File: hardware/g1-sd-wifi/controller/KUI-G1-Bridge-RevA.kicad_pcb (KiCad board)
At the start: 6 copper layers, 59 x 115 mm, 351 parts, among them J10 FPGA JTAG pogo pads, J20 5V/GND direct wire pads, J201 microSD push-pull 1.42mm, J202 RP USB service pads, J203 RP SWD/reset/boot pads, J204 C5 direct UART recovery pads, J40 FH12-14S-0.5SH(55), J41 FH12-6S-0.5SH(55), J50 FH12-20S-0.5SH(55), J51 FH12-20S-0.5SH(55), K201 C5 removable compression cont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, K202 C5 removable compression cont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, K203 C5 removable compression cont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, K204 C5 removable compression cont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, K205 C5 removable compression cont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, K206 C5 removable compression cont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, K207 C5 removable compression cont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, K208 C5 removable compression cont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, K209 C5 removable compression cont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, K210 C5 removable compression cont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, K211 C5 removable compression cont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, K212 C5 removable compression cont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, K213 C5 removable compression cont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, K214 C5 removable compression cont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, K215 C5 removable compression cont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, K216 C5 removable compression cont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, Q20 PMV48XP reverse polarity, Q201 C5 recovery pull-down, Q202 C5 recovery pull-down, U10 LCMXO2-2000HC-4TG100C, U20 TPS2116 automatic mux, U201 RP2350B, U202 16MiB boot NOR, U203 8MiB QSPI PSRAM, U204 C5 off-state isolation, U205 C5 off-state isolation, U207 SD4-bit DAT rail isolation, U208 SD CLK/CMD rail isolation, U209 SD enable/power-good NAND, U21 TPS62162 3.3V 1A, U22 TPS62162 3.3V 1A, U23 TPS3808G33DBVR, U24 TPS3808G33DBVR, U25 TPS3808G33DBVR, U26 TPS3808G01DBVR, U27 SN74LVC2G08DCUR, U28 SN74LVC2G08DCUR, U29 SN74LVC2G08DCUR, U30 SN74LVC1G11DBVR, U31 SN74LVC2G04DBVT, U32 SN74LVC1G32DBVR, U33 SN74LVC1G08DBVR, U34 SN74LVC1G08DBVR, U35 SN74LVC16T245, U36 SN74LVC244A host controls, U37 SN74LVC1G17 host RESETn, U38 SN74LVC1G125 qualified ATA_IN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, U39 SN74LVC1G125 qualified ATA_DM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, U40 MX29LV640ETTI-70G x8 / 4 x 2M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, U41 SN74LVC2G125 bank-domain buff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, U42 SN74LVC1G11 write-authorize A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, U43 SN74LVC1G04 write-block inver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, U44 SN74LVC1G332 NOR WE qualifier, U45 TLV803EB29 console-rail NOR r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, U70 SN74LVC1G07 open-drain IORDY, U71 TPS22919 Wi-Fi input switch, U72 SN74LVC1G32DBVR, U73 SN74LVC1G32DBVR, X10 50MHz 3.3V, X201 12MHz

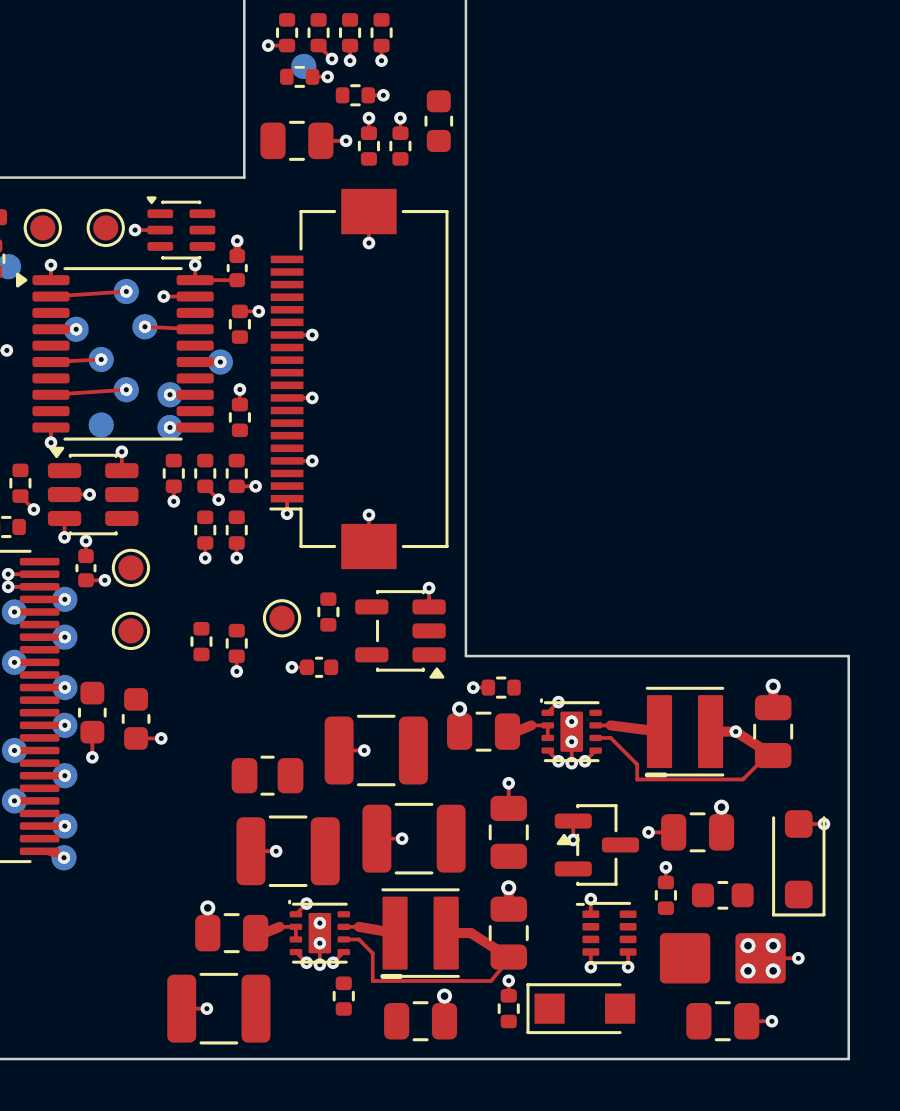
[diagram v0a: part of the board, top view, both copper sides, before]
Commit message: G1 safety: supply trunks laid first; current checker no longer passes vacuously
check_power_copper.py joined a track end that met another segment to both
of that segment's ends, collapsing most supply nets into a single node: the
source and loads merged, every branch carried 0 A and the check passed. The
copper graph now splits a track where another end or via lands on it, and
the 2x pad-escape allowance applies only to a short run that starts at a
pad, not to every short segment of a long track. On the last routed
snapshot this exposes the 1.3 A input path at 0.25-0.30 mm (about 25 C rise)
and a 0.2 mm via carrying the PRIMARY_5V trunk.

route_power_trunks.py now lays the high-current trunks on the placed board
before signal routing, locked: J20 -> F20 -> Q20 at 1.0 mm on F.Cu with no
via, F20 -> D21 at 0.8 mm, Q20 -> U20 at 0.5 mm with a short neck at the
fine-pitch pin, Q20 -> U71/C235 and Q20 -> C200 at 0.6-0.8 mm, as a tree.
C208 moves 1.2 mm towards L20 to open the input corridor.

Routing rules go to 0.127 mm track and space (0.15 mm stalled near 20 open
connections). close_gaps.py takes its rules from the project, rasterises
obstacles at the right cell offset (Pillow samples pixel centres at +0.5),
routes supply gaps only at supply widths with POWER vias, refills zones in
its DRC check, never saves a board without its project file, and gains a
rip-up mode in which each attempt is kept only if native DRC shows fewer
open connections and no new violation. The finishing script fails if the
project rules file changes.

Co-Authored-By: Claude Opus 5.5 <noreply@anthropic.com>
Claude-Session: https://claude.ai/code/session_01Gp9EYc2r9fMpZ7V8WtfonZ
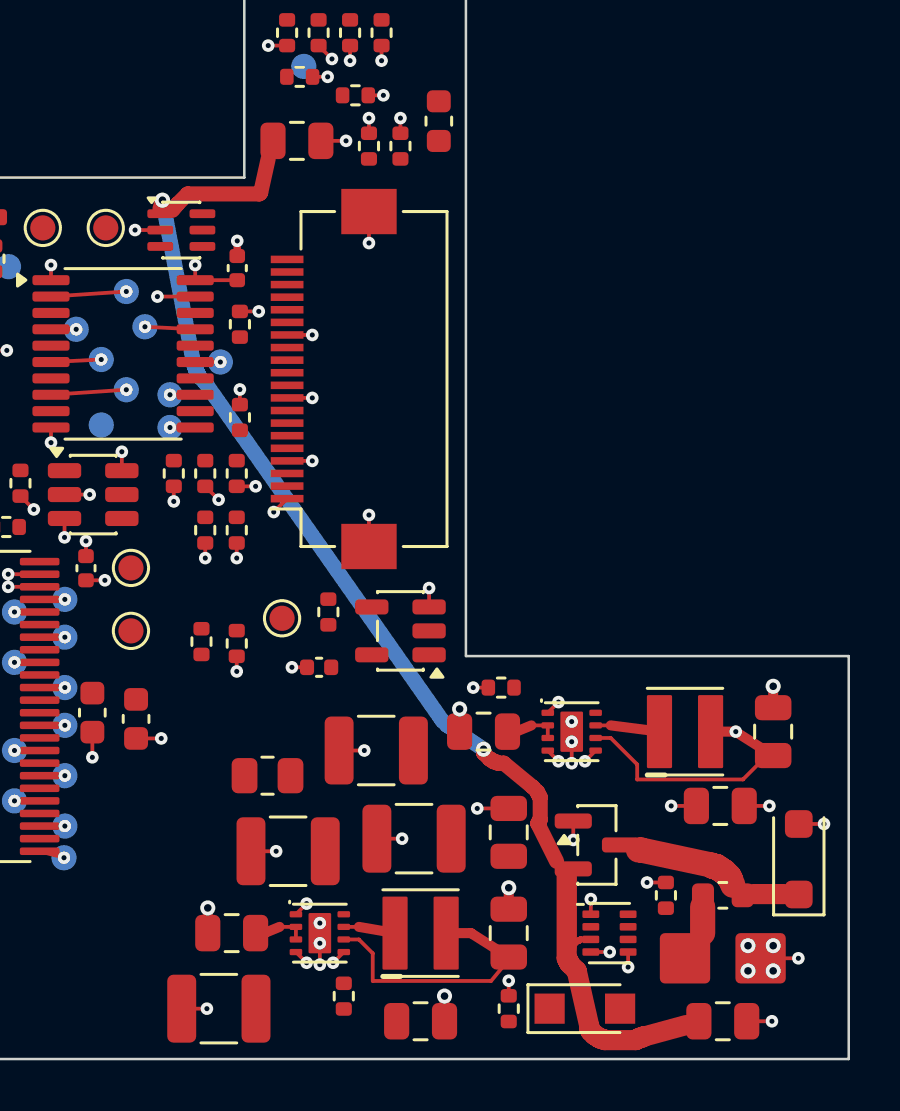
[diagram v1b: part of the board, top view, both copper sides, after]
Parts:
- moved C208 1.38 mm to (123.9, 149.9)
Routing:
- net PRIMARY_5V: track 0.00 -> 51.3 mm, vias 0 -> 2
- net FUSED_5V: track 0.00 -> 5.49 mm
- net CONSOLE_5V: track 0.00 -> 1.05 mm
- net GND: track 220.4 -> 221.2 mm

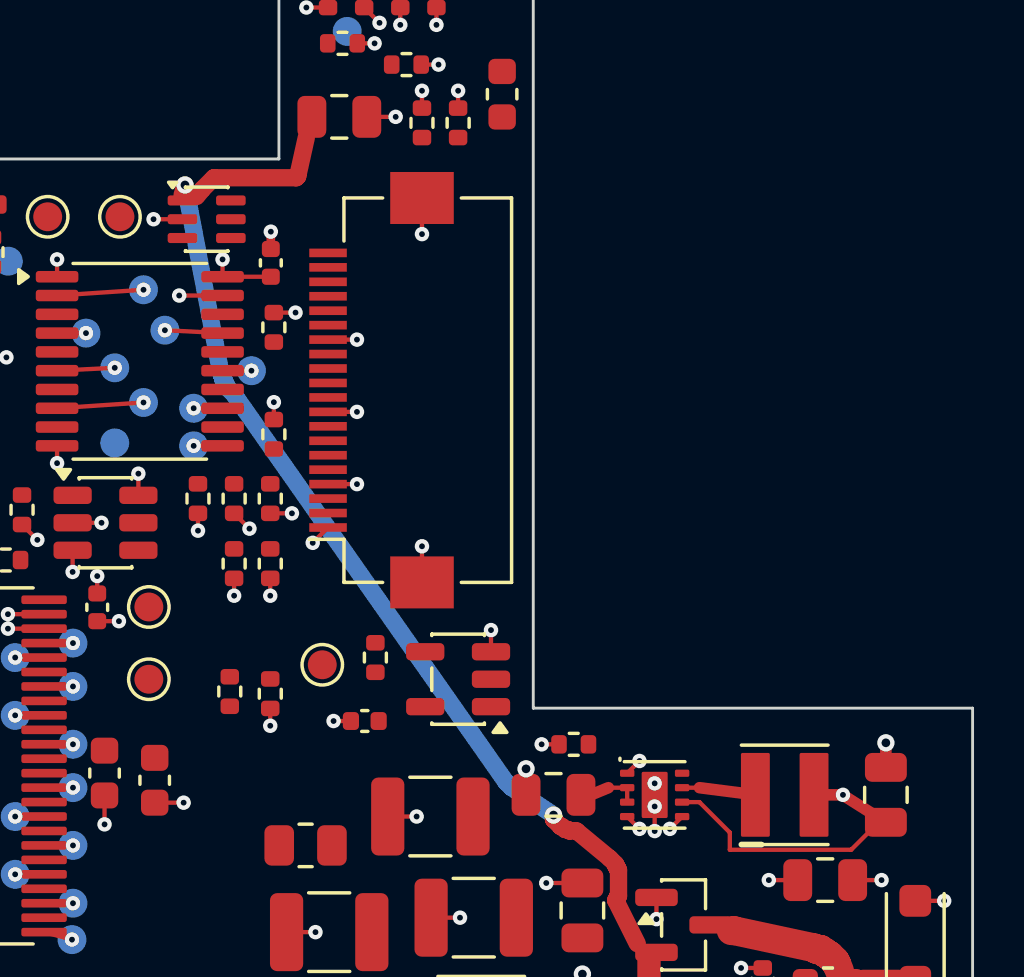
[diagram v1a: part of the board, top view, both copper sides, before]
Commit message: G1: resumable routing checkpoint; plane feed vias; rip-up can move vias
design/routing-checkpoint/ holds the board's DSN, the best routed session
and the SHA-256 of the board it belongs to; tools/route_carrier.sh starts,
resumes, saves and finishes from it, so a new session or container carries
on instead of routing again. design/ROUTING-CHECKPOINT.md records the state
and the remaining steps.

The +3V3_LOGIC plane was fed from L20.2 through one 0.2 mm via, about
108 C over ambient at the converter's assumed 1.5 A short-circuit current.
route_power_trunks.py now adds three 0.3 mm feed vias beside the pad (not
in it, so no solder is drawn from the joint), and check_power_copper.py
rates the plane feed at that fault current. close_gaps.py keeps new vias
0.1 mm clear of every SMD land, and its rip-up attempts may cut vias as
well as tracks, rerouting what native DRC then reports open.

Co-Authored-By: Claude Opus 5.5 <noreply@anthropic.com>
Claude-Session: https://claude.ai/code/session_01Gp9EYc2r9fMpZ7V8WtfonZ
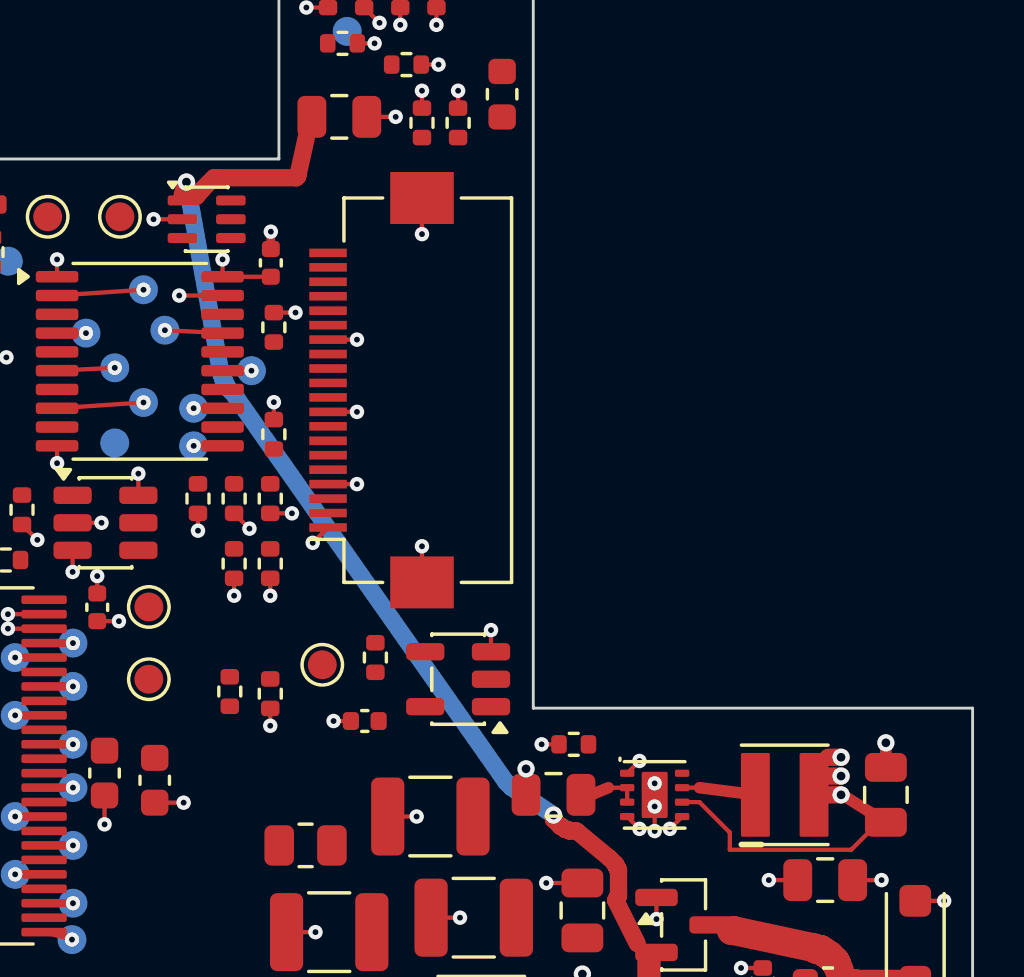
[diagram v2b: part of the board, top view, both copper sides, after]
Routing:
- net +3V3_LOGIC: track 145.3 -> 145.6 mm, vias 121 -> 123

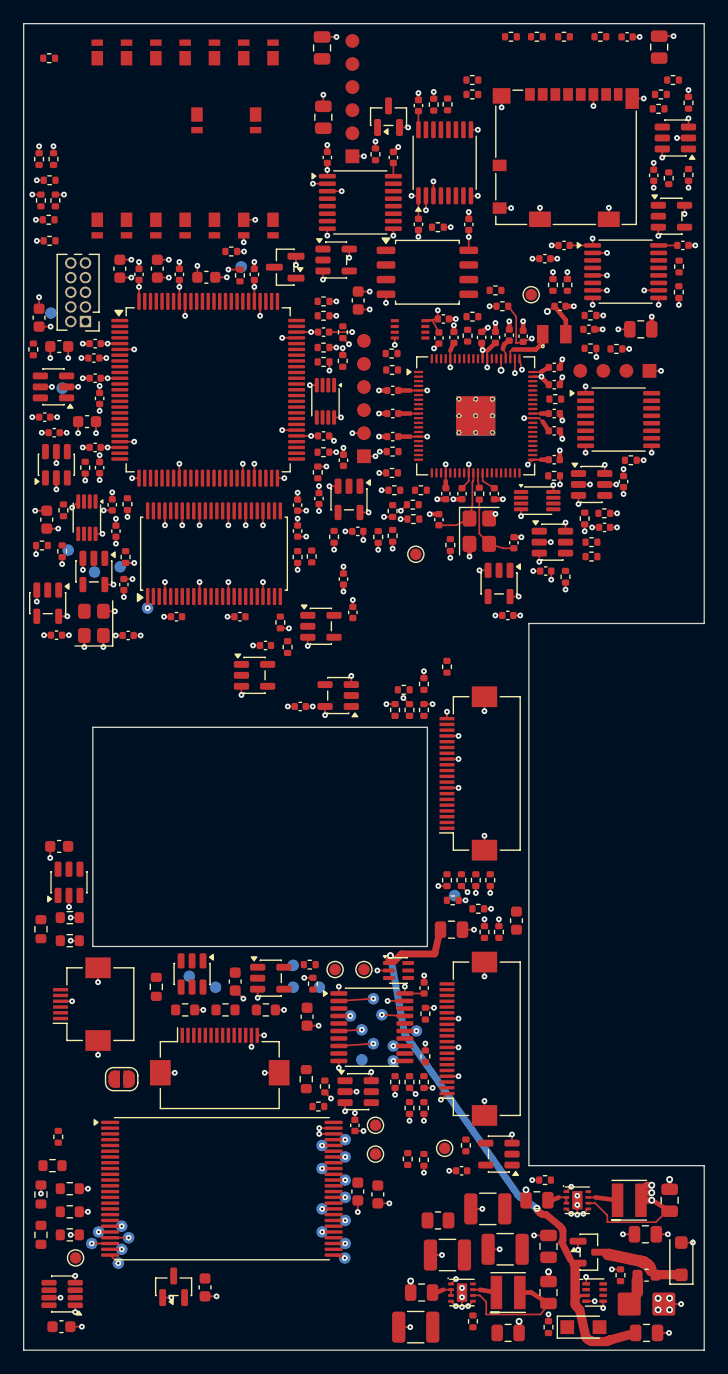
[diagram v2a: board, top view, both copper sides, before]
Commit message: G1 floorplan: FPGA -> U36 control bundle laid first; trunk and probes clear U36
Every routing run left four or five of the eight FPGA -> U36 host-control
lines open. Their FPGA pins face a column of bypass capacitors, and U36's
east pin row (0.65 mm pitch, 3 mm from J51) had raw-probe lands under its
body and the PRIMARY_5V trunk beneath it on B.Cu, so the lines had nowhere
to drop through.

- route_bus_bundle.py lays the bundle on the six-layer board before the
  autorouter, locked: escapes inward under the TQFP, down the west corridor
  and under the BIOS opening, kept off U35 and the J50 corridor. Seven of
  eight lines go in; BUS_DA2 is left to the router.
- route_power_trunks.py keeps trunks out of U36 and runs Q20 -> C235 ->
  U71 up the corridor east of J51 instead.
- add_carrier_raw_probes.py staggers U36's probes west and keeps them out
  of the west half of its body; the floorplan re-places all nine.

The placed board is DRC clean with schematic parity 0; the routing
checkpoint is reset to it.

Co-Authored-By: Claude Opus 5.5 <noreply@anthropic.com>
Claude-Session: https://claude.ai/code/session_01Gp9EYc2r9fMpZ7V8WtfonZ
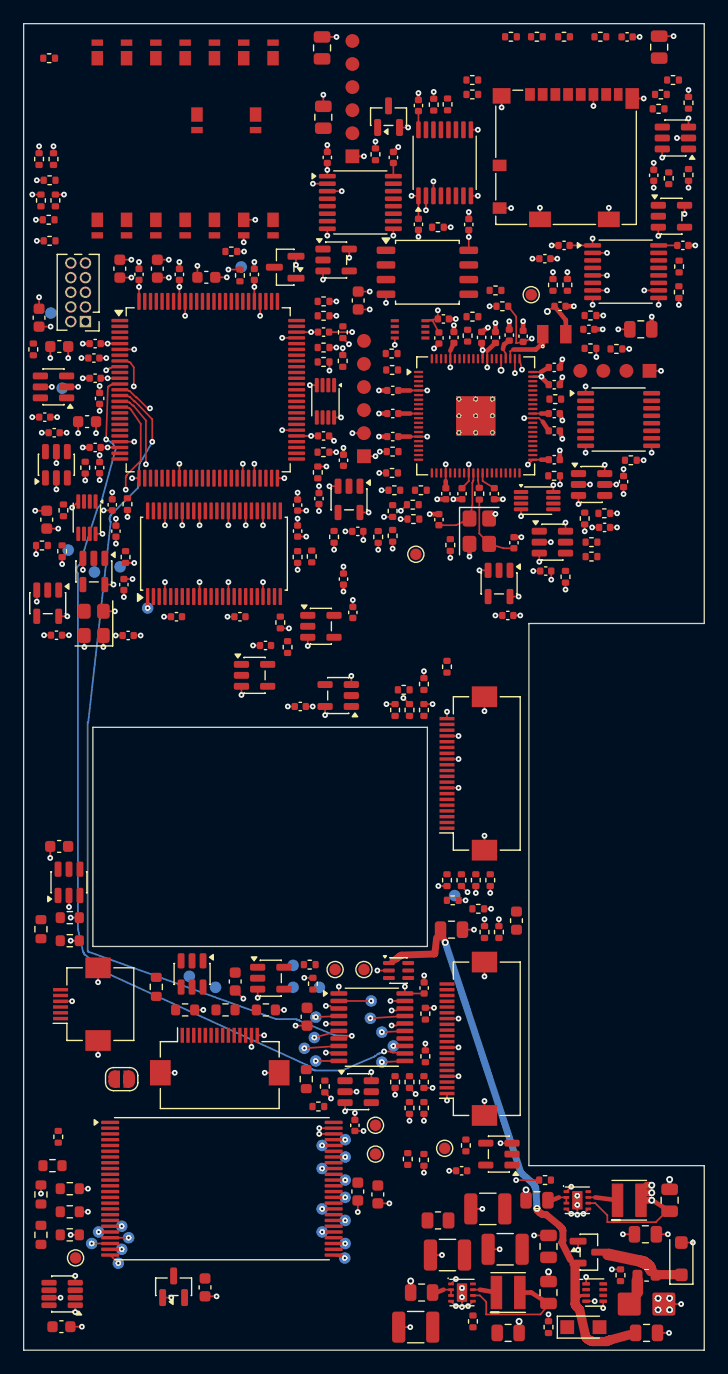
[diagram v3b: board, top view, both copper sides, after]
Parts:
- moved TP119 5.99 mm to (94.3, 133.8)
- moved TP118 4.17 mm to (95.2, 132.9)
- moved TP137 4.00 mm to (95.3, 134.9)
- moved TP117 3.00 mm to (95.3, 131.1)
- moved TP122 3.00 mm to (101.1, 132.4)
- moved TP124 1.04 mm to (100.1, 131.2)
- moved TP120 1.00 mm to (101.1, 135.0)
- moved TP116 0.28 mm to (100.1, 129.7)
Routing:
- net BUS_DA1: track 0.00 -> 84.0 mm, vias 0 -> 2
- net BUS_DA0: track 0.00 -> 81.6 mm, vias 0 -> 2
- net BUS_CS0n: track 0.00 -> 80.8 mm, vias 0 -> 2
- net BUS_CS1n: track 0.00 -> 75.3 mm, vias 0 -> 2
- net BUS_DIORn: track 0.00 -> 75.2 mm, vias 0 -> 2
- net BUS_DIOWn: track 0.00 -> 72.2 mm, vias 0 -> 2
- net BUS_DMACKn: track 0.00 -> 70.3 mm, vias 0 -> 2
- net +3V3_LOGIC: track 145.6 -> 147.0 mm
- net PRIMARY_5V: track 51.5 -> 50.1 mm
- net GND: track 221.2 -> 222.4 mm
- net ATA_DMACKn: track 2.00 -> 3.00 mm
- net ATA_DA1: track 1.00 -> 2.00 mm
- net ATA_CS1n: track 1.00 -> 2.00 mm
- net ATA_DIOWn: track 1.00 -> 2.00 mm

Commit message: G1 carrier: routed board replaces the placed one; outputs regenerated
controller/KUI-G1-Bridge-RevA.kicad_pcb is now the fully routed carrier
(SHA-256 7d7c3d26...). Native DRC with zones refilled, all severities:
0 violations, 0 unconnected, schematic parity 0. The supply copper
current check passes (design/power-copper-check.json); the DRC report is
design/carrier-final-drc.json.

On the finished board every plane hop was tried again with the
exhaustive search limited to the signal layers. ATA_DD6's moved back;
the other nine (120 mm on In4.Cu, all in the corridors beside the BIOS
opening) have no way there and stay. The In4 plane fills as one island.

Regenerated from this board: BASE and BASE_PSRAM_DNP BOM/CPL drafts
(only C2016 and R2038 move), the 1:1 fit sheets, and the release
preflight (still blocked on the owner reviews and D21/F21 catalog
numbers, as it must be). check_integration --check, check_flex and the
manufacturing tests pass.

design/CARRIER-LAYOUT-REVIEW.md is rewritten for this board, including
how the last connections were closed and the plane hops for the owner
to review. Routing checkpoint, owner steps and manufacturing status
updated; part counts in the manufacturing README corrected to the
generated drafts (264 BASE SMT parts, 52 of 54 types with exact catalog
identities). The finishing checkpoint board is removed: the routed
board lives in controller/.

Co-Authored-By: Claude Opus 5.5 <noreply@anthropic.com>
Claude-Session: https://claude.ai/code/session_01Gp9EYc2r9fMpZ7V8WtfonZ
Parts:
- moved C2016 2.42 mm to (108.5, 72.0)
- moved R2038 2.41 mm to (110.9, 72.0)
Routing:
- net CONSOLE_3V3: track 0.00 -> 296.1 mm, vias 0 -> 7
- net +3V3_STORAGE: track 12.8 -> 213.5 mm, vias 0 -> 5
- net BIOS_BANK0: track 0.00 -> 173.9 mm, vias 0 -> 15
- net ATA_DD8: track 1.00 -> 172.6 mm, vias 1 -> 9
- net IORDY_RELEASE: track 0.00 -> 159.0 mm, vias 0 -> 13
- net +5V_C5: track 0.00 -> 150.1 mm, vias 0 -> 12
- net ATA_CS0n: track 3.00 -> 147.9 mm, vias 1 -> 10
- net ATA_DD0: track 1.00 -> 127.2 mm, vias 1 -> 5
- net BUS_SAFE: track 0.00 -> 119.5 mm, vias 0 -> 10
- net ATA_DD14: track 1.00 -> 120.1 mm, vias 1 -> 10
- net ATA_DD15: track 1.00 -> 112.8 mm, vias 1 -> 5
- net ATA_DD13: track 1.60 -> 110.8 mm, vias 1 -> 6
- net ATA_DD12: track 1.60 -> 109.3 mm, vias 1 -> 6
- net PWR_FAILn: track 0.00 -> 104.8 mm, vias 0 -> 5
- net ATA_DD11: track 1.00 -> 104.2 mm, vias 1 -> 6
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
